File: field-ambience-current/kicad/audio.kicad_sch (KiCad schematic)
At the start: 26 parts, among them J6 Speaker L (PUI AS04008PS, 4R 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, J7 Speaker R (PUI AS04008PS, 4R 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, U3 PCM5102A I²S DAC (TSSOP-20), U4 PAM8403H Class-D Stereo Amp (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

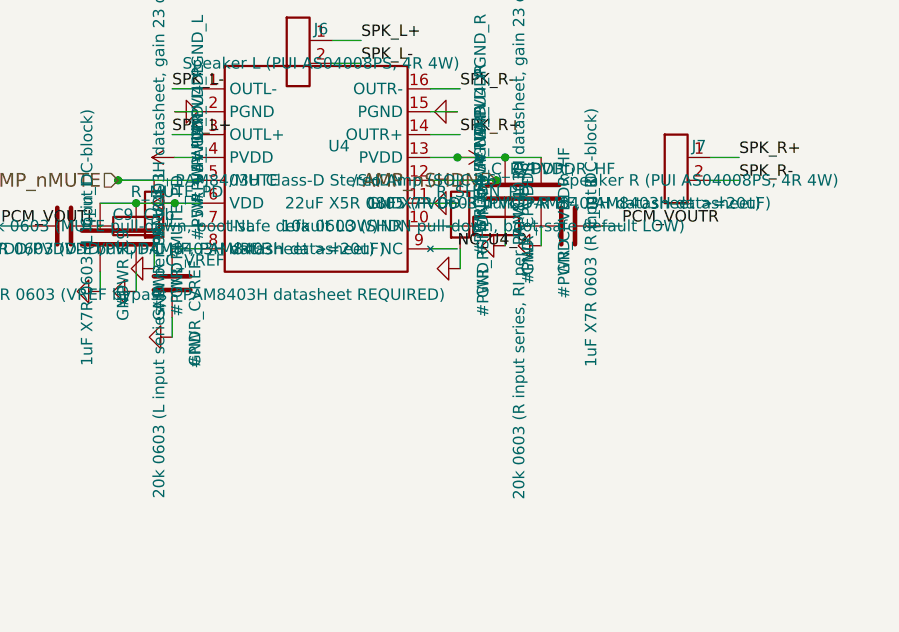
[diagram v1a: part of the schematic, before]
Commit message: v0.7-pre: Choc V2 footprint fix + Line-Out/Headphone block (J8)
Two real design improvements requested after the device evaluation.

=== 1. Switch footprint mismatch fixed (Choc V2) ===

BUG: generator referenced Button_Switch_Keyboard:SW_Hotswap_Kailh_MX_*
(MX hotswap) while BOM/SPEC specify Kailh Choc V2 throughout. MX and
Choc V2 are physically incompatible (pin spacing, height, keycap stem).
Building the MX footprint with Choc V2 sockets → parts don't fit.

FIX: footprints → Switch_Keyboard_Hotswap_Kailh:SW_Hotswap_Kailh_Choc_V1V2_*
(1.00u modifiers, 2.00u cells). Verified: 0 MX refs remain, 10 Choc refs.

LIBRARY: these are NOT in KiCad standard libs. Requires the kiswitch
keyswitch-kicad-library (PCM → Libraries → "Keyswitch Kicad Library").
Documented in SPEC §4, PCB_TODO B0, CHANGELOG. Exact footprint name must
be verified after install (B0 blocker).

=== 2. Line-Out / Headphone block (J8) — fixes the "deep character" problem ===

The 40mm onboard speakers physically cannot reproduce the 30-60Hz SubBass
the Sound Constitution is built around. Without an external output the
device's core character stays trapped in the box.

Hardware (Sheet 6 audio extended):
- J8: 3.5mm TRS jack with insertion-detect switch (PJ-320 class, C2884109)
- Passive tap from PCM5102A VOUTL/VOUTR BEFORE the PAM8403. PCM5102A output
  is ground-centered (internal charge pump) → no coupling caps needed.
- R_LO_L / R_LO_R: 22Ω series (short-circuit protection, C22962)
- Jack-detect: J8 DET switch → MCP23017 GPA6 (pull-up + IRQ enabled).
  Idle (no plug) = LOW, inserted = HIGH.

Firmware:
- New AudioPower.speakers(on) method separates speaker-amp mute from full
  system mute. Jack insert → mute ONLY the PAM8403; PCM5102A DAC + line-out
  stay live. Speaker and line-out are mutually exclusive (plug = speakers off).
- read_buttons() now reads GPA6, tracks jack state, emits {"event":"jack",
  "inserted":bool}, calls amp.speakers(not inserted) locally.
- {"set":"amp"} command now calls speake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
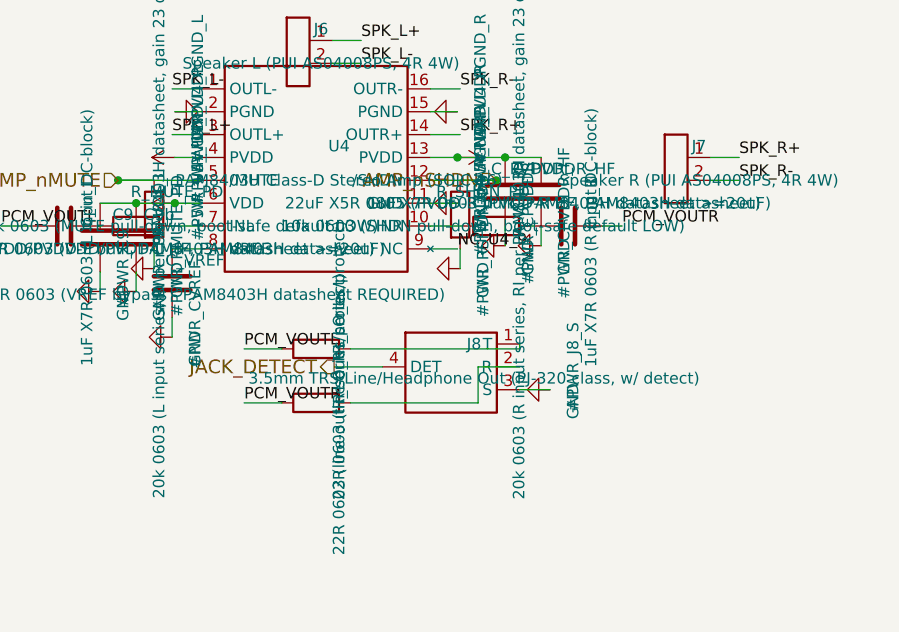
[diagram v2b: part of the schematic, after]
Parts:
- added J8: 3.5mm TRS Line/Headphone Out (PJ-320 class, w/ de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, Connector_Audio:Jack_3.5mm_CUI_SJ-3523-SMT_Horizontal, symbol Connector:AudioJack3_Switch
- added R_LO_L: 22R 0603 (line-out L series/protect), Resistor_SMD:R_0603_1608Metric, symbol Device:R
- added R_LO_R: 22R 0603 (line-out R series/protect), Resistor_SMD:R_0603_1608Metric, symbol Device:R
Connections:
- net GND: now also J8.3 (S)
- net PCM_VOUTL: now also R_LO_L.1
- net PCM_VOUTR: now also R_LO_R.1
- new net: J8.1 (T), R_LO_L.2
- new net: J8.2 (R), R_LO_R.2
- new net JACK_DETECT: J8.4 (DET)
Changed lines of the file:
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@@
       (project "field_ambience"
         (path "/66fcdc89-be06-4d61-a855-abf9641d963c" (reference "J7") (unit 1)))))
+  (symbol (lib_id "Device:R") (at 160 150.0 90) (unit 1)
+    (in_bom yes) (on_board yes) (dnp no)
+      (property "Reference" "R_LO_L" (at 162.54 147.46 0)
+        (effects (font (size 1.27 1.27))))
+      (property "Value" "22R 0603 (line-out L series/protect)" (at 162.54 151.27 0)
+        (effects (font (size 1.27 1.27))))
+      (property "Footprint" "Resistor_SMD:R_0603_1608Metric" (at 160 150.0 0)
+        (effects (font (size 1.27 1.27)) hide))
+      (property "Datasheet" "~" (at 160 150.0 0)
+        (effects (font (size 1.27 1.27)) hide))
+      (property "MPN" "RC0603FR-0722RL" (at 162.54 153.81 0)
+        (effects (font (size 1.27 1.27)) hide))
+      (property "LCSC" "C22962" (at 162.54 155.08 0)
+        (effects (font (size 1.27 1.27)) hide))
+    (instances
+      (project "field_ambience"
+        (path "/66fcdc89-be06-4d61-a855-abf9641d963c" (reference "R_LO_L") (unit 1)))))
+  (symbol (lib_id "Device:R") (at 160 156.0 90) (unit 1)
+    (in_bom yes) (on_board yes) (dnp no)
+      (property "Reference" "R_LO_R" (at 162.54 153.46 0)
+        (effects (font (size 1.27 1.27))))
+      (property "Value" "22R 0603 (line-out R series/protect)" (at 162.54 157.27 0)
+        (effects (font (size 1.27 1.27))))
+      (property "Footprint" "Resistor_SMD:R_0603_1608Metric" (at 160 156.0 0)
+        (effects (font (size 1.27 1.27)) hide))
+      (property "Datasheet" "~" (at 160 156.0 0)
+        (effects (font (size 1.27 1.27)) hide))
+      (property "MPN" "RC0603FR-0722RL" (at 162.54 159.81 0)
+        (effects (font (size 1.27 1.27)) hide))
+      (property "LCSC" "C22962" (at 162.54 161.08 0)
+        (effects (font (size 1.27 1.27)) hide))
+    (instances
+      (project "field_ambience"
+        (path "/66fcdc89-be06-4d61-a855-abf9641d963c" (reference "R_LO_R") (unit 1)))))
+  (symbol (lib_id "Connector:AudioJack3_Switch") (at 175.0 152.0 0) (unit 1)
+    (in_bom yes) (on_board yes) (dnp no)
+      (property "Reference" "J8" (at 177.54 149.46 0)
+        (effects (font (size 1.27 1.27))))
+      (property "Value" "3.5mm TRS Line/Headphone Out (PJ-320 class, w/ detect)" (at 177.54 153.27 0)
+        (effects (font (size 1.27 1.27))))
+      (property "Footprint" "Connector_Audio:Jack_3.5mm_CUI_SJ-3523-SMT_Horizontal" (at 175.0 152.0 0)
+        (effects (font (size 1.27 1.27)) hide))
+      (property "Datasheet" "~" (at 175.0 152.0 0)
+        (effects (font (size 1.27 1.27)) hide))
+      (property "MPN" "PJ-320D o.ä. (TRS w/ switch)" (at 177.54 155.81 0)
+        (effects (font (size 1.27 1.27)) hide))
+      (property "LCSC" "C2884109" (at 177.54 157.08 0)
+        (effects (font (size 1.27 1.27)) hide))
+    (instances
+      (project "field_ambience"
+        (path "/66fcdc89-be06-4d61-a855-abf9641d963c" (reference "J8") (unit 1)))))
+  (symbol (lib_id "Power:GND") (at 186 154.54 270) (unit 1)
+    (in_bom yes) (on_board yes) (dnp no)
+      (property "Reference" "#PWR_J8_S" (at 188.54 152.0 0)
+        (effects (font (size 1.27 1.27))))
+      (property "Value" "GND" (at 188.54 155.81 0)
+        (effects (font (size 1.27 1.27))))
+      (property "Footprint" "" (at 186 154.54 0)
+        (effects (font (size 1.27 1.27)) hide))
+      (property "Datasheet" "~" (at 186 154.54 0)
+        (effects (font (size 1.27 1.27)) hide))
+    (instances
+      (project "field_ambience"
+        (path "/66fcdc89-be06-4d61-a855-abf9641d963c" (reference "#PWR_J8_S") (unit 1)))))
   (wire (pts (xy 87.3 88.57) (xy 84.3 88.57))
     (stroke (width 0) (type default))
@@
     (stroke (width 0) (type default))
 )
+  (wire (pts (xy 156.19 150.0) (xy 152 150.0))
+    (stroke (width 0) (type default))
+)
+  (wire (pts (xy 156.19 156.0) (xy 152 156.0))
+    (stroke (width 0) (type default))
+)
+  (wire (pts (xy 163.81 150.0) (xy 182.62 150.0))
+    (stroke (width 0) (type default))
+)
+  (wire (pts (xy 182.62 150.0) (xy 182.62 149.46))
+    (stroke (width 0) (type default))
+)
+  (wire (pts (xy 163.81 156.0) (xy 178 156.0))
+    (stroke (width 0) (type default))
+)
+  (wire (pts (xy 178 156.0) (xy 178 152))
+    (stroke (width 0) (type default))
+)
+  (wire (pts (xy 178 152) (xy 182.62 152))
+    (stroke (width 0) (type default))
+)
+  (wire (pts (xy 182.62 154.54) (xy 186 154.54))
+    (stroke (width 0) (type default))
+)
+  (wire (pts (xy 167.38 152) (xy 162 152))
+    (stroke (width 0) (type default))
+)
   (junction (at 84.3 88.57) (diameter 0) (color 0 0 0 0)
 )
@@
     (effects (font (size 1.27 1.27)) (justify left bottom))
 )
+  (label "PCM_VOUTL" (at 152 150.0 0) (fields_autoplaced)
+    (effects (font (size 1.27 1.27)) (justify left bottom))
+)
+  (label "PCM_VOUTR" (at 152 156.0 0) (fields_autoplaced)
+    (effects (font (size 1.27 1.27)) (justify left bottom))
+)
   (hierarchical_label "I2S_BCK" (shape input) (at 120 106.35 180)
     (effects (font (size 1.524 1.524)) (justify right))
@@
     (effects (font (size 1.524 1.524)) (justify right))
 )
+  (hierarchical_label "JACK_DETECT" (shape output) (at 162 152 0)
+    (effects (font (size 1.524 1.524)) (justify right))
+)

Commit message: fix(bom): make entire BOM correctly JLC-orderable — 7 real part errors fixed
Verified every LCSC number against jlcsearch for existence, stock, AND that
it resolves to the intended value/package. Found 7 parts that would have
built WRONG or were unorderable:

CRITICAL value/package errors (LCSC pointed at the wrong part):
- R_VOL_L/R: C25092 = 22ohm 0402  -> C4184  (real 20k 0603, Basic).
  Was wrong value AND footprint; would have wrecked the PAM8403 input gain.
- R_LO_L/R:  C22962 = 220ohm       -> C23345 (real 22ohm 0603, Basic).
- R_BCK/LRCK/DOUT: C23138 = 330ohm -> C23140 (real 33ohm 0603, Basic).

Unorderable -> assigned real in-stock parts:
- J8 jack:  C2884109 (nonexistent) -> C431535 (PJ-320D SMD).
- C_BULK:   placeholder            -> C46550395 (1000uF 16V SMD D10x10.5).
- LED1:     no LCSC                -> C965818 (white 0805).
- R1:       C22548 Extended        -> C21190 Basic (prior commit).

Also aligned all MPN text to the actual LCSC part (Yageo text vs Uni Royal/
Samsung parts JLC ships) so the BOM is internally consistent.

Re-verified: 25 distinct LCSC, all in stock, ZERO value/package mismatches,
14 Basic / 11 Extended. SPEC §4 stale refs (C_BULK/J8/R_LO) updated.
MEINE_TODO Abschnitt 0 rewritten with the full orderability result.

Self-supply parts (Pico, OLED, speakers, Choc sockets, EC11, headers) keep
no LCSC by design — JLC cannot assemble those.

https://claude.ai/code/session_01K5kLTFpDCCoYwx2dq6RkAv
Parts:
- C9b, C_FLY, C_PVDDR_HF, C_VNEG, C_VREF, C_in_L, C_in_R: MPN CC0603KRX7R7BB105 -> CL10A105KB8NNNC
- J8: LCSC C2884109 -> C431535; MPN PJ-320D o.ä. (TRS w/ switch) -> PJ-320D (3.5mm TRS w/ switch)
- R_LO_L, R_LO_R: LCSC C22962 -> C23345; MPN RC0603FR-0722RL -> 0603WAF220JT5E
- R_MUTE_PD, R_SHDN_PD, R_XSMT_PD: MPN RC0603FR-0710KL -> 0603WAF1002T5E
- R_VOL_L, R_VOL_R: LCSC C25092 -> C4184; MPN RC0603FR-0720KL -> 0603WAF2002T5E
- U4: MPN PAM8403H -> PAM8403DR-H
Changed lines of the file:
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@@
       (property "Datasheet" "~" (at 82 93.65 0)
         (effects (font (size 1.27 1.27)) hide))
-      (property "MPN" "CC0603KRX7R7BB105" (at 84.54 97.46000000000001 0)
+      (property "MPN" "CL10A105KB8NNNC" (at 84.54 97.46000000000001 0)
         (effects (font (size 1.27 1.27)) hide))
       (property "LCSC" "C15849" (at 84.54 98.73 0)
@@
       (property "Datasheet" "~" (at 78 102.53999999999999 0)
         (effects (font (size 1.27 1.27)) hide))
-      (property "MPN" "CC0603KRX7R7BB105" (at 80.54 106.35 0)
+      (property "MPN" "CL10A105KB8NNNC" (at 80.54 106.35 0)
         (effects (font (size 1.27 1.27)) hide))
       (property "LCSC" "C15849" (at 80.54 107.61999999999999 0)
@@
       (property "Datasheet" "~" (at 132 100.0 0)
         (effects (font (size 1.27 1.27)) hide))
-      (property "MPN" "RC0603FR-0710KL" (at 134.54 103.81 0)
+      (property "MPN" "0603WAF1002T5E" (at 134.54 103.81 0)
         (effects (font (size 1.27 1.27)) hide))
       (property "LCSC" "C25804" (at 134.54 105.08 0)
@@
       (property "Datasheet" "PAM8403H.PDF (Diodes Inc Rev 1-0, Nov 2012)" (at 160.0 130.0 0)
         (effects (font (size 1.27 1.27)) hide))
-      (property "MPN" "PAM8403H" (at 162.54 133.81 0)
+      (property "MPN" "PAM8403DR-H" (at 162.54 133.81 0)
         (effects (font (size 1.27 1.27)) hide))
       (property "LCSC" "C17337" (at 162.54 135.08 0)
@@
       (property "Datasheet" "~" (at 142 135.08 0)
         (effects (font (size 1.27 1.27)) hide))
-      (property "MPN" "RC0603FR-0710KL" (at 144.54 138.89000000000001 0)
+      (property "MPN" "0603WAF1002T5E" (at 144.54 138.89000000000001 0)
         (effects (font (size 1.27 1.27)) hide))
       (property "LCSC" "C25804" (at 144.54 140.16000000000003 0)
@@
       (property "Datasheet" "~" (at 140 137.62 0)
         (effects (font (size 1.27 1.27)) hide))
-      (property "MPN" "CC0603KRX7R7BB105" (at 142.54 141.43 0)
+      (property "MPN" "CL10A105KB8NNNC" (at 142.54 141.43 0)
         (effects (font (size 1.27 1.27)) hide))
       (property "LCSC" "C15849" (at 142.54 142.70000000000002 0)
@@
       (property "Datasheet" "~" (at 140 136.35 0)
         (effects (font (size 1.27 1.27)) hide))
-      (property "MPN" "RC0603FR-0720KL" (at 142.54 140.16 0)
-        (effects (font (size 1.27 1.27)) hide))
-      (property "LCSC" "C25092" (at 142.54 141.43 0)
+      (property "MPN" "0603WAF2002T5E" (at 142.54 140.16 0)
+        (effects (font (size 1.27 1.27)) hide))
+      (property "LCSC" "C4184" (at 142.54 141.43 0)
         (effects (font (size 1.27 1.27)) hide))
     (instances
@@
       (property "Datasheet" "~" (at 132 136.35 0)
         (effects (font (size 1.27 1.27)) hide))
-      (property "MPN" "CC0603KRX7R7BB105" (at 134.54 140.16 0)
+      (property "MPN" "CL10A105KB8NNNC" (at 134.54 140.16 0)
         (effects (font (size 1.27 1.27)) hide))
       (property "LCSC" "C15849" (at 134.54 141.43 0)
@@
       (property "Datasheet" "~" (at 144 142.7 0)
         (effects (font (size 1.27 1.27)) hide))
-      (property "MPN" "CC0603KRX7R7BB105" (at 146.54 146.51 0)
+      (property "MPN" "CL10A105KB8NNNC" (at 146.54 146.51 0)
         (effects (font (size 1.27 1.27)) hide))
       (property "LCSC" "C15849" (at 146.54 147.78 0)
@@
       (property "Datasheet" "~" (at 180 136.35 0)
         (effects (font (size 1.27 1.27)) hide))
-      (property "MPN" "RC0603FR-0720KL" (at 182.54 140.16 0)
-        (effects (font (size 1.27 1.27)) hide))
-      (property "LCSC" "C25092" (at 182.54 141.43 0)
+      (property "MPN" "0603WAF2002T5E" (at 182.54 140.16 0)
+        (effects (font (size 1.27 1.27)) hide))
+      (property "LCSC" "C4184" (at 182.54 141.43 0)
         (effects (font (size 1.27 1.27)) hide))
     (instances
@@
       (property "Datasheet" "~" (at 188 136.35 0)
         (effects (font (size 1.27 1.27)) hide))
-      (property "MPN" "CC0603KRX7R7BB105" (at 190.54 140.16 0)
+      (property "MPN" "CL10A105KB8NNNC" (at 190.54 140.16 0)
         (effects (font (size 1.27 1.27)) hide))
       (property "LCSC" "C15849" (at 190.54 141.43 0)
@@
       (property "Datasheet" "~" (at 176 135.08 0)
         (effects (font (size 1.27 1.27)) hide))
-      (property "MPN" "RC0603FR-0710KL" (at 178.54 138.89000000000001 0)
+      (property "MPN" "0603WAF1002T5E" (at 178.54 138.89000000000001 0)
         (effects (font (size 1.27 1.27)) hide))
       (property "LCSC" "C25804" (at 178.54 140.16000000000003 0)
@@
       (property "Datasheet" "~" (at 185 132.54 0)
         (effects (font (size 1.27 1.27)) hide))
-      (property "MPN" "CC0603KRX7R7BB105" (at 187.54 136.35 0)
+      (property "MPN" "CL10A105KB8NNNC" (at 187.54 136.35 0)
         (effects (font (size 1.27 1.27)) hide))
       (property "LCSC" "C15849" (at 187.54 137.62 0)
@@
       (property "Datasheet" "~" (at 160 150.0 0)
         (effects (font (size 1.27 1.27)) hide))
-      (property "MPN" "RC0603FR-0722RL" (at 162.54 153.81 0)
-        (effects (font (size 1.27 1.27)) hide))
-      (property "LCSC" "C22962" (at 162.54 155.08 0)
+      (property "MPN" "0603WAF220JT5E" (at 162.54 153.81 0)
+        (effects (font (size 1.27 1.27)) hide))
+      (property "LCSC" "C23345" (at 162.54 155.08 0)
         (effects (font (size 1.27 1.27)) hide))
     (instances
@@
       (property "Datasheet" "~" (at 160 156.0 0)
         (effects (font (size 1.27 1.27)) hide))
-      (property "MPN" "RC0603FR-0722RL" (at 162.54 159.81 0)
-        (effects (font (size 1.27 1.27)) hide))
-      (property "LCSC" "C22962" (at 162.54 161.08 0)
+      (property "MPN" "0603WAF220JT5E" (at 162.54 159.81 0)
+        (effects (font (size 1.27 1.27)) hide))
+      (property "LCSC" "C23345" (at 162.54 161.08 0)
         (effects (font (size 1.27 1.27)) hide))
     (instances
@@
       (property "Datasheet" "~" (at 175.0 152.0 0)
         (effects (font (size 1.27 1.27)) hide))
-      (property "MPN" "PJ-320D o.ä. (TRS w/ switch)" (at 177.54 155.81 0)
-        (effects (font (size 1.27 1.27)) hide))
-      (property "LCSC" "C2884109" (at 177.54 157.08 0)
-        (effects (font (size 1.27 1.27)) hide))
-    (instances
+      (property "MPN" "PJ-320D (3.5mm TRS w/ switch)" (at 177.54 155.81 0)
+        (effects (font (size 1.27 1.27)) hide))
+      (property "LCSC" "C431535" (at 177.54 157.08 0)
+        (effects (font (size 1.27 1.27)) hide))
+    (instances
